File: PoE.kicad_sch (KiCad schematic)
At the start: 81 parts, among them Q2 BSZ440N10NS3GATMA1, T1 PA2467NL, U23 TPS23734, U24 TCMT1107

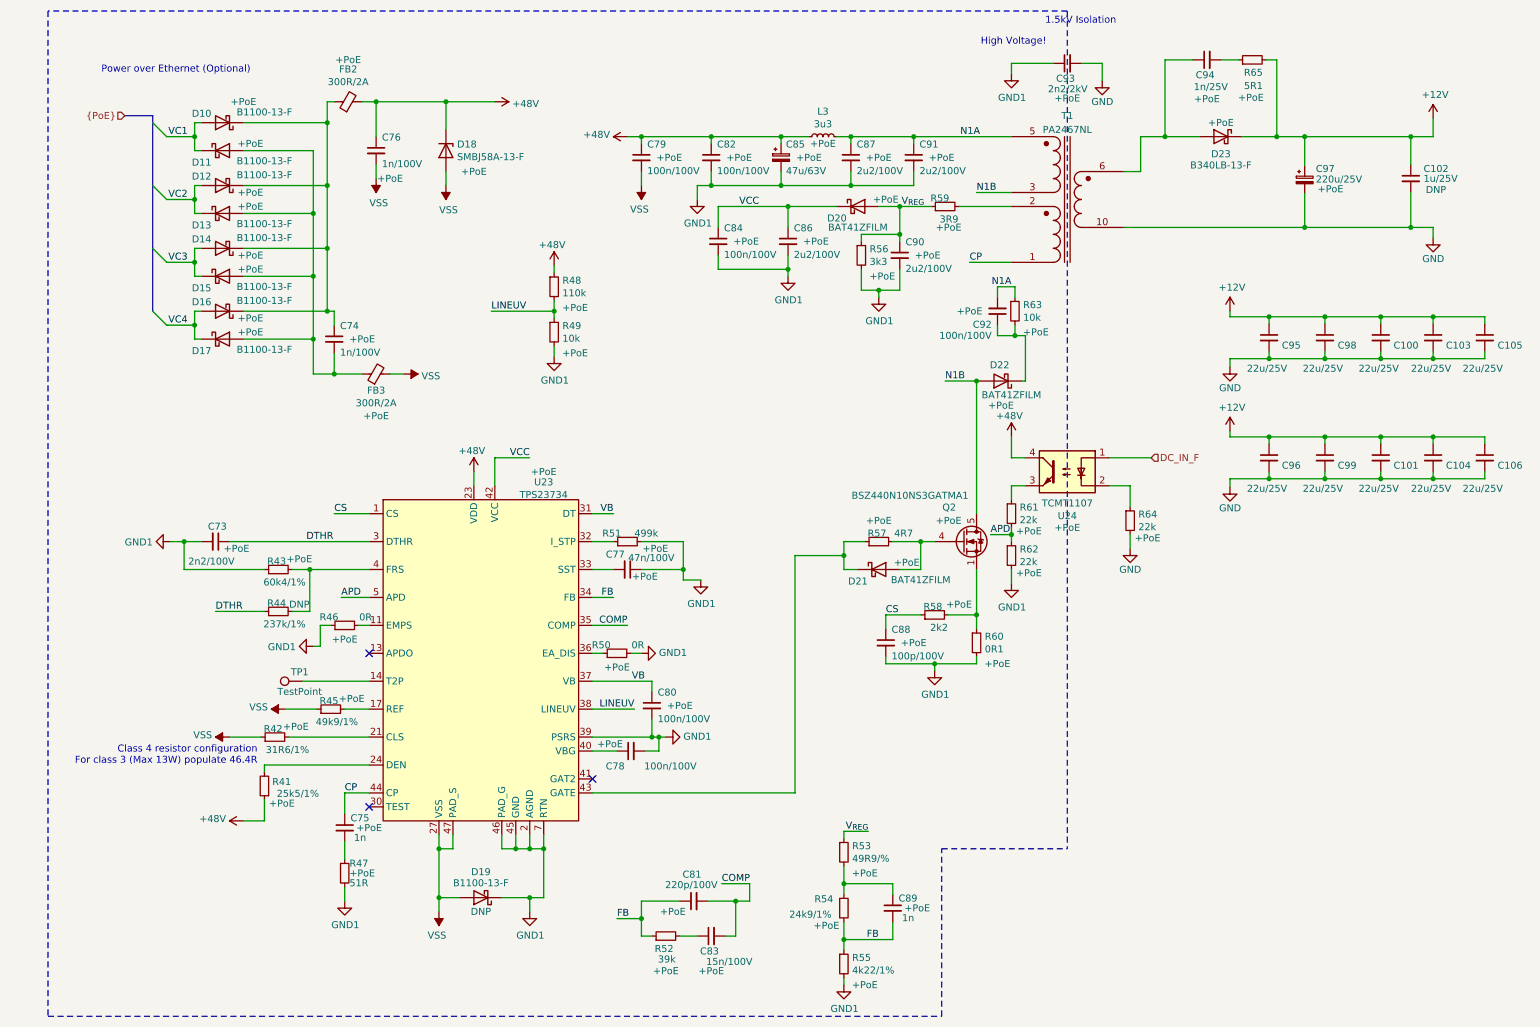
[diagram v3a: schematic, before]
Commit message: Adjust rating/footprint size of some ceramic capacitors
Also update connector/jumper designator to make more sense.

Signed-off-by: Stefan Agner <stefan@agner.ch>
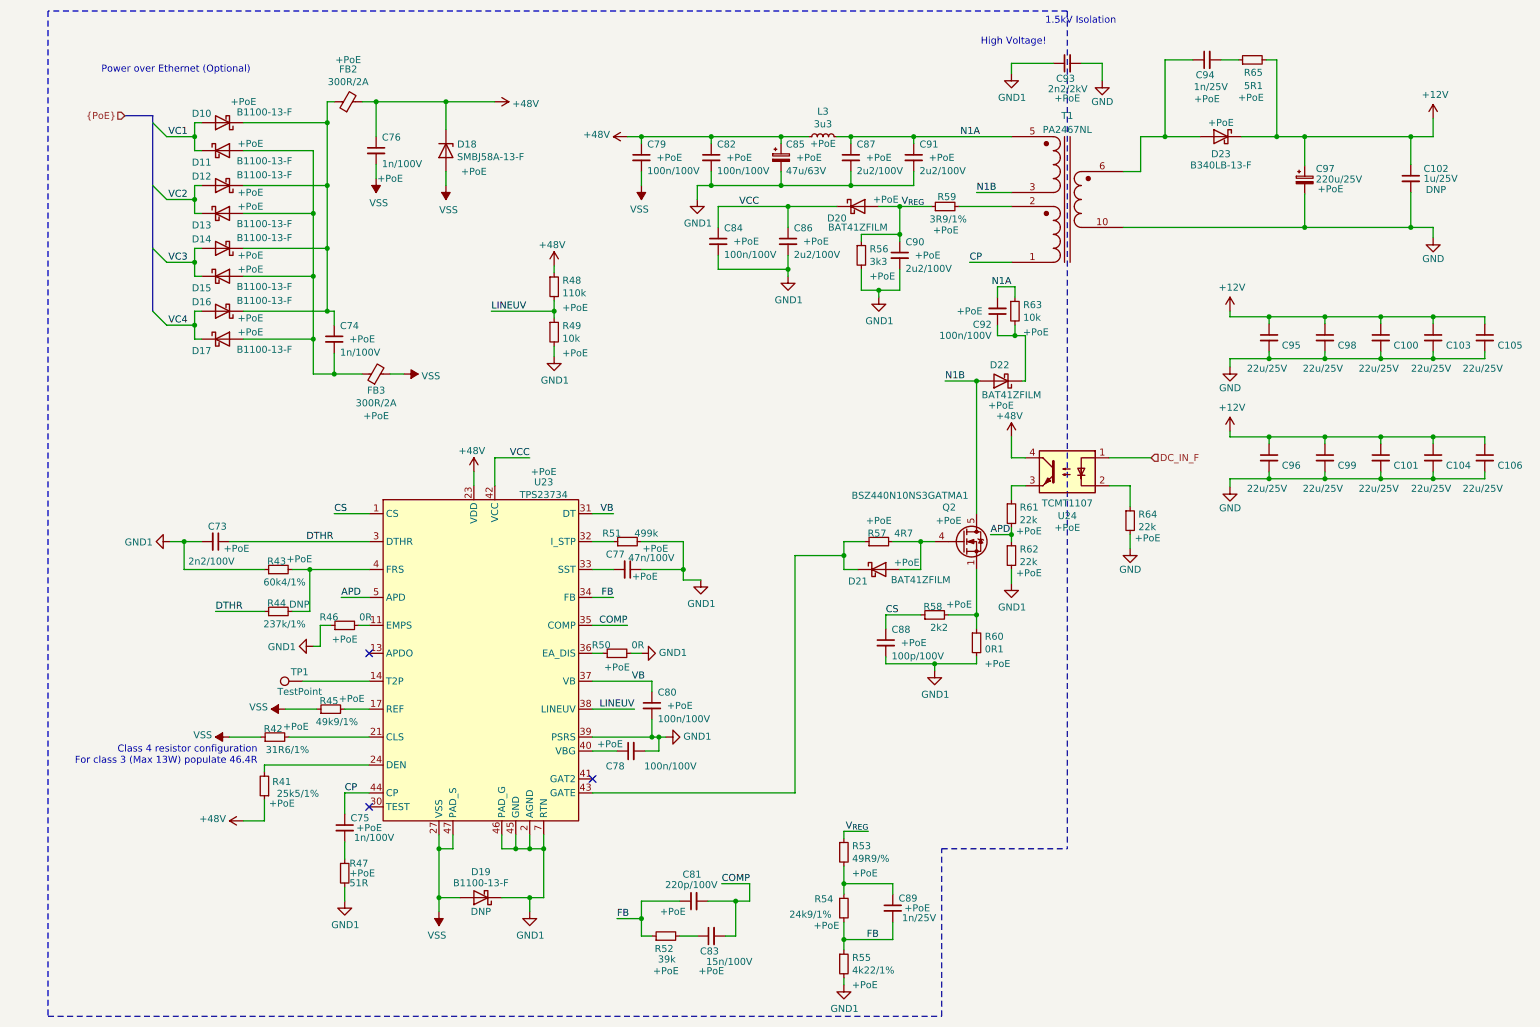
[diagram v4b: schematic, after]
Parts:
- C75: value 1n -> 1n/100V; footprint Capacitor_SMD:C_0402_1005Metric -> Capacitor_SMD:C_0805_2012Metric
- C89: value 1n -> 1n/25V
- C93: footprint Capacitor_SMD:C_0402_1005Metric -> Capacitor_SMD:C_1812_4532Metric
- R59: value 3R9 -> 3R9/1%; footprint Resistor_SMD:R_1206_3216Metric -> Resistor_SMD:R_0805_2012Metric
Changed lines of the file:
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@@
   (symbol (lib_id "Device:R_Small") (at 177.165 48.26 90) (unit 1)
     (in_bom yes) (on_board yes)
-    (property "Reference" "R59" (id 0) (at 177.9206 46.7613 90)
-      (effects (font (size 1.27 1.27)) (justify left))
-    )
-    (property "Value" "3R9" (id 1) (at 179.584 50.571 90)
-      (effects (font (size 1.27 1.27)) (justify left))
-    )
-    (property "Footprint" "Resistor_SMD:R_1206_3216Metric" (id 2) (at 177.165 48.26 0)
+    (property "Reference" "R59" (id 0) (at 179.1906 46.5073 90)
+      (effects (font (size 1.27 1.27)) (justify left))
+    )
+    (property "Value" "3R9/1%" (id 1) (at 181.108 50.571 90)
+      (effects (font (size 1.27 1.27)) (justify left))
+    )
+    (property "Footprint" "Resistor_SMD:R_0805_2012Metric" (id 2) (at 177.165 48.26 0)
       (effects (font (size 1.27 1.27)) hide)
     )
@@
       (effects (font (size 1.27 1.27)) hide)
     )
-    (property "Config" "+PoE" (id 4) (at 177.8 52.07 90))
+    (property "Config" "+PoE" (id 4) (at 177.292 52.578 90))
     (pin "1")
     (pin "2")
@@
       (effects (font (size 1.27 1.27)) (justify left))
     )
-    (property "Value" "1n" (id 1) (at 69.634 163.074 0)
-      (effects (font (size 1.27 1.27)) (justify left))
-    )
-    (property "Footprint" "Capacitor_SMD:C_0402_1005Metric" (id 2) (at 67.945 161.29 0)
+    (property "Value" "1n/100V" (id 1) (at 69.634 163.074 0)
+      (effects (font (size 1.27 1.27)) (justify left))
+    )
+    (property "Footprint" "Capacitor_SMD:C_0805_2012Metric" (id 2) (at 67.945 161.29 0)
       (effects (font (size 1.27 1.27)) hide)
     )
@@
       (effects (font (size 1.27 1.27)) (justify left))
     )
-    (property "Value" "1n" (id 1) (at 169.329 177.679 0)
+    (property "Value" "1n/25V" (id 1) (at 169.329 177.679 0)
       (effects (font (size 1.27 1.27)) (justify left))
     )
@@
       (effects (font (size 1.27 1.27)) (justify left))
     )
-    (property "Footprint" "Capacitor_SMD:C_0402_1005Metric" (id 2) (at 199.39 22.225 0)
-      (effects (font (size 1.27 1.27)) hide)
-    )
+    (property "Footprint" "Capacitor_SMD:C_1812_4532Metric" (id 2) (at 199.39 22.225 0)
+      (effects (font (size 1.27 1.27)) hide)
+    )

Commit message: Add PG-TSDSON-8-1 package for Infineon BSZ440N10NS3
Add package for Infineon N-Channel MOSFET BSZ440N10NS3.

Signed-off-by: Stefan Agner <stefan@agner.ch>
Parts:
- Q2: footprint Package_TO_SOT_SMD:TDSON-8-1 -> LightBlue:PG-TSDSON-8
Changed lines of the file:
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@@
       (effects (font (size 1.27 1.27)) (justify left))
     )
-    (property "Footprint" "Package_TO_SOT_SMD:TDSON-8-1" (id 2) (at 185.42 111.125 0)
+    (property "Footprint" "LightBlue:PG-TSDSON-8" (id 2) (at 185.42 111.125 0)
       (effects (font (size 1.27 1.27) italic) (justify left) hide)
     )
-    (property "Datasheet" "http://www.infineon.com/dgdl/Infineon-BSC440N10NS3-DS-v02_04-en.pdf?fileId=db3a30432239cccd0122604520d47f56" (id 3) (at 180.34 109.22 90)
+    (property "Datasheet" "https://www.infineon.com/dgdl/Infineon-BSZ440N10NS3%20G-DS-v02_01-EN.pdf?fileId=db3a304320896aa20120c32dbf312354" (id 3) (at 180.34 109.22 90)
       (effects (font (size 1.27 1.27)) (justify left) hide)
     )

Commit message: Add footprint for Pulse PA2467NL transformer
Signed-off-by: Stefan Agner <stefan@agner.ch>
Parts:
- T1: footprint LightBlue:Transformer_EPQ-13 -> LightBlue:Transformer_Pulse_PA2467NL
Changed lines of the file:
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@@
     (property "Reference" "T1" (id 0) (at 199.39 31.75 0))
     (property "Value" "PA2467NL" (id 1) (at 199.39 34.29 0))
-    (property "Footprint" "LightBlue:Transformer_EPQ-13" (id 2) (at 199.39 45.72 0)
+    (property "Footprint" "LightBlue:Transformer_Pulse_PA2467NL" (id 2) (at 199.39 45.72 0)
       (effects (font (size 1.27 1.27)) hide)
     )

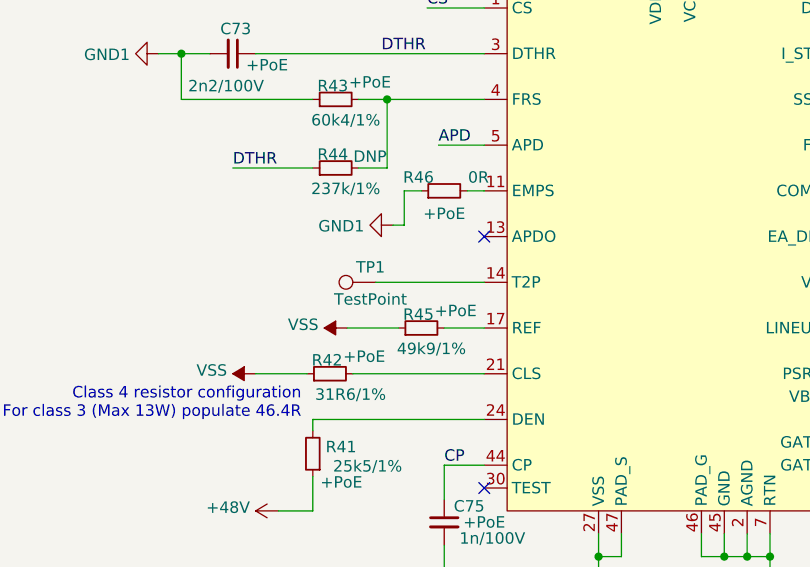
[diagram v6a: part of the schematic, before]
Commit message: pcb 0.2:
Changes:
Footrints:
-Modified DC Jack to accomodate CUI PJ-002A
-Modified RJ45 to increase clearance between shield and poe pins
-Modified m.2 mounting pads to avoid drc errors
Schematic:
-usb-c facing usb mux is supplied by +3v3VP
-added misc. capacitors
PCB
-min. annular ring for vias set to 0.125 from 0.2

Signed-off-by: Dominik Sliwa <dominik@sliwa.io>
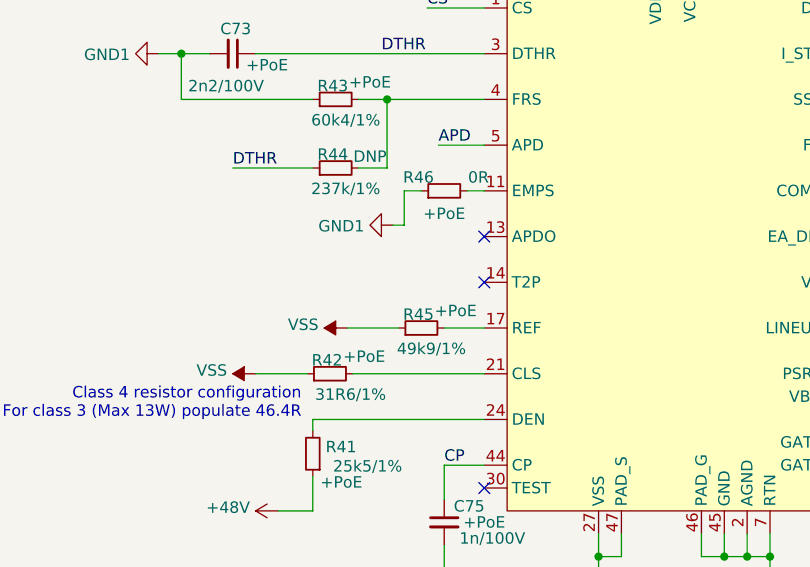
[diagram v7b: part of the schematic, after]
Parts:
- removed TP1: TestPoint, TestPoint:TestPoint_Pad_D1.0mm, symbol Connector:TestPoint
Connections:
- no-connect marks 3 -> 4
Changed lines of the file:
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@@
   (junction (at 265.938 97.79) (diameter 0.9144) (color 0 0 0 0))
   (no_connect (at 72.39 129.54))
+  (no_connect (at 72.39 134.62))
   (no_connect (at 72.39 157.48))
   (no_connect (at 113.03 152.4))
@@
     (stroke (width 0) (type solid) (color 0 0 0 0))
   )
-  (wire (pts (xy 60.325 134.62) (xy 72.39 134.62))
-    (stroke (width 0) (type solid) (color 0 0 0 0))
-  )
   (wire (pts (xy 61.595 114.3) (xy 72.39 114.3))
     (stroke (width 0) (type solid) (color 0 0 0 0))
@@
     (pin "2")
   )
-  (symbol (lib_id "Connector:TestPoint") (at 60.325 134.62 90) (unit 1)
-    (in_bom yes) (on_board yes)
-    (property "Reference" "TP1" (id 0) (at 59.7535 132.9498 90))
-    (property "Value" "TestPoint" (id 1) (at 59.7535 136.5185 90))
-    (property "Footprint" "TestPoint:TestPoint_Pad_D1.0mm" (id 2) (at 60.325 129.54 0)
-      (effects (font (size 1.27 1.27)) hide)
-    )
-    (property "Datasheet" "~" (id 3) (at 60.325 129.54 0)
-      (effects (font (size 1.27 1.27)) hide)
-    )
-    (pin "1")
-  )
   (symbol (lib_id "power:GND1") (at 36.195 109.22 270) (unit 1)

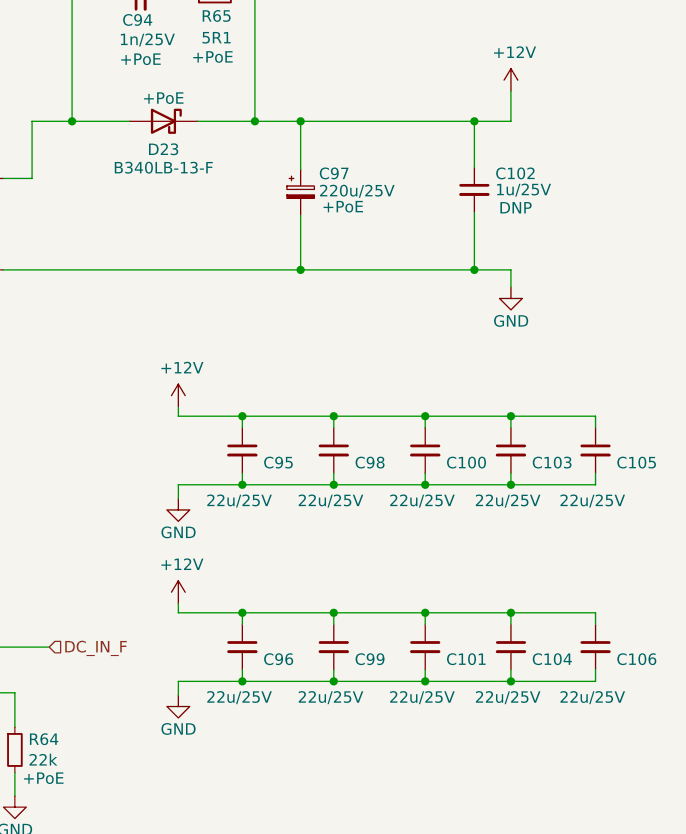
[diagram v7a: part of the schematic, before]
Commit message: Update silkscreen/adjust reference designators
Order some relevant reference designator. Use JP for all jumpers. Place
silkcreen neatly. Add some custom silk screen. Remove heat sink corner
marks on silk screen.

Signed-off-by: Stefan Agner <stefan@agner.ch>
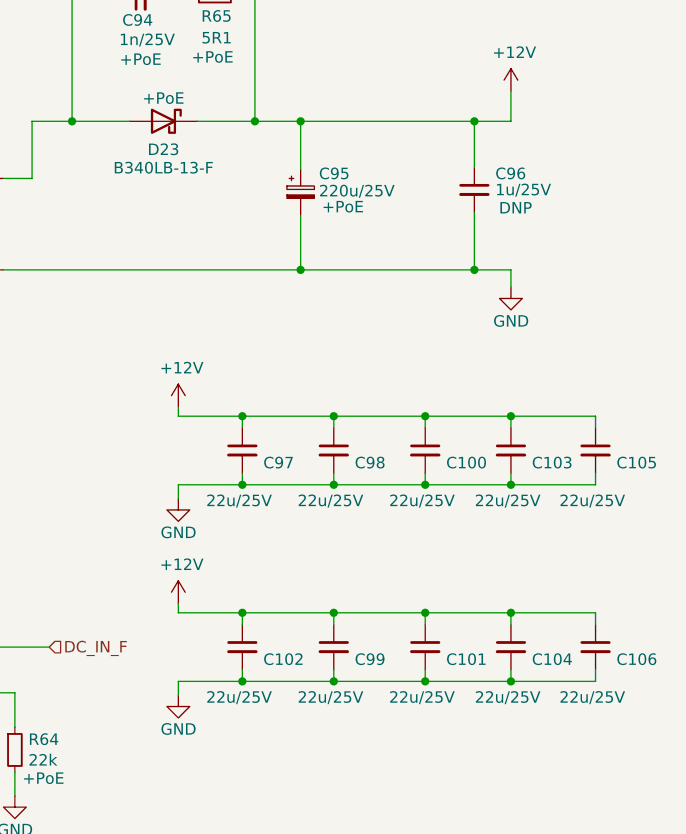
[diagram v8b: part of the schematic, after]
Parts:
- renumbered C96 to C102, C97 to C95, C102 to C96, C95 to C97
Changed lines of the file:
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@@
   (symbol (lib_id "Device:CP_Small") (at 242.57 43.434 0) (unit 1)
     (in_bom yes) (on_board yes)
-    (property "Reference" "C97" (id 0) (at 244.6021 41.3956 0)
+    (property "Reference" "C95" (id 0) (at 244.6021 41.3956 0)
       (effects (font (size 1.27 1.27)) (justify left))
     )
@@
   (symbol (lib_id "Device:C_Small") (at 236.093 72.136 0) (unit 1)
     (in_bom yes) (on_board yes)
-    (property "Reference" "C95" (id 0) (at 238.4172 73.5266 0)
+    (property "Reference" "C97" (id 0) (at 238.4172 73.5266 0)
       (effects (font (size 1.27 1.27)) (justify left))
     )
@@
   (symbol (lib_id "Device:C_Small") (at 236.093 93.98 0) (unit 1)
     (in_bom yes) (on_board yes)
-    (property "Reference" "C96" (id 0) (at 238.4172 95.3706 0)
+    (property "Reference" "C102" (id 0) (at 238.4172 95.3706 0)
       (effects (font (size 1.27 1.27)) (justify left))
     )
@@
   (symbol (lib_id "Device:C_Small") (at 261.874 43.18 0) (unit 1)
     (in_bom yes) (on_board yes)
-    (property "Reference" "C102" (id 0) (at 264.1982 41.3956 0)
-      (effects (font (size 1.27 1.27)) (justify left))
-    )
+    (property "Reference" "C96" (id 0) (at 264.1982 41.3956 0)
+      (effects (font (size 1.27 1.27)) (justify left))
+    )
